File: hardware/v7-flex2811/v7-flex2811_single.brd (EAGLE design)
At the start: 7.8 x 7.8 mm, 8 parts

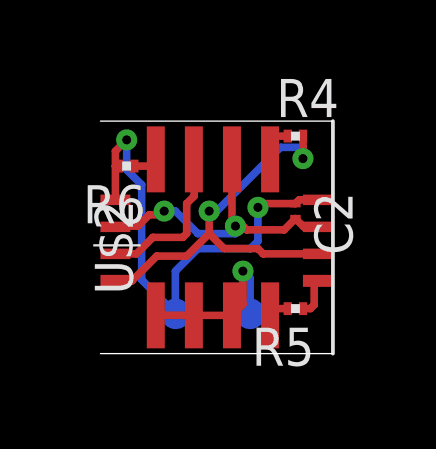
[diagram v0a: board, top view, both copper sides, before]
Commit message: Rework the single for more clearance to make fab easier
Was concerned about how tight the passives were for
assmebly, have just spread it out a bit

Also made the WS2818 pads slightly smaller so we have more clearance
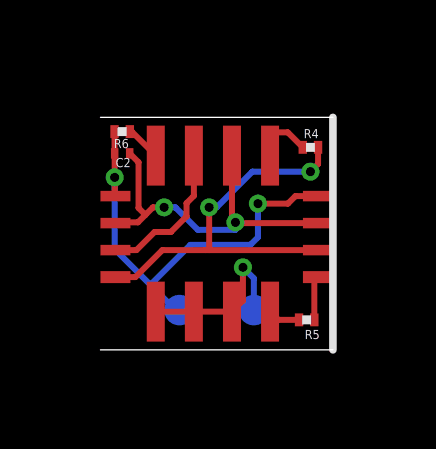
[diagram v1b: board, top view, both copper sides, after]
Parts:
- U$2: device adafruit:SO08 -> Sparky:SO08
- moved C2 6.09 mm to (0.72, 6.55), turned to 0 degrees
- moved R6 1.16 mm to (0.72, 7.28)
- moved R4 0.62 mm to (7.00, 6.75)
- moved R5 0.53 mm to (6.88, 1.00)
- moved U$1 0.18 mm to (3.88, 3.88)
- moved U$2 0.12 mm to (3.75, 3.88)
- moved U$3 0.12 mm to (0.50, 2.12)
- moved U$4 0.12 mm to (7.25, 2.12)
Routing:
- net GND: track 10.2 -> 12.1 mm
- net VCC: track 16.6 -> 15.0 mm
- net N$4: track 1.56 -> 2.27 mm

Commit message: More edit for manufacturability
Add a preliminary BOM
Add labels for the ICs for assembly
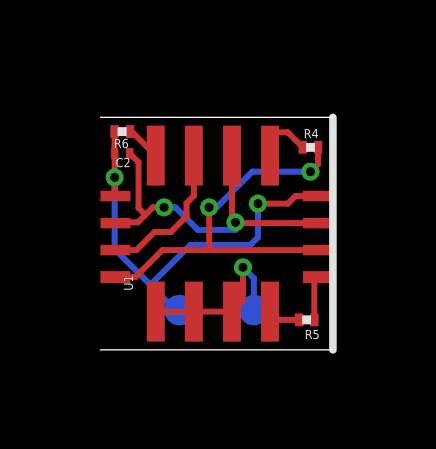
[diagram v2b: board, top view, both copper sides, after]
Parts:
- C2: value (none) -> 0.1uF
- R4, R5: value (none) -> 33Ω
- R6: value (none) -> 100Ω
- renumbered U$1 to P1, U$2 to U1
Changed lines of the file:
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@@
 <layer number="25" name="tNames" color="7" fill="1" visible="yes" active="yes"/>
 <layer number="26" name="bNames" color="7" fill="1" visible="yes" active="yes"/>
-<layer number="27" name="tValues" color="7" fill="1" visible="yes" active="yes"/>
-<layer number="28" name="bValues" color="7" fill="1" visible="yes" active="yes"/>
+<layer number="27" name="tValues" color="7" fill="1" visible="no" active="yes"/>
+<layer number="28" name="bValues" color="7" fill="1" visible="no" active="yes"/>
 <layer number="29" name="tStop" color="7" fill="3" visible="no" active="yes"/>
 <layer number="30" name="bStop" color="7" fill="6" visible="no" active="yes"/>
@@
 </autorouter>
 <elements>
-<element name="C2" library="rcl" package="C0201" value="" x="0.725" y="6.55" smashed="yes">
+<element name="C2" library="rcl" package="C0201" value="0.1uF" x="0.725" y="6.55" smashed="yes">
 <attribute name="NAME" x="0.505" y="6.09" size="0.3048" layer="25" font="vector" ratio="15"/>
 <attribute name="VALUE" x="0.09" y="4.645" size="1.27" layer="27"/>
 </element>
-<element name="U$1" library="tom-tappytap-v5-flex" package="TP_4MM_MED_PAD" value="TP_4MM_MED_PAD" x="3.875" y="3.875" smashed="yes" rot="MR0"/>
-<element name="U$2" library="Sparky" package="SO08" value="WS2818" x="3.75" y="3.875" smashed="yes"/>
-<element name="R4" library="rcl" package="R0201" value="" x="7" y="6.75" smashed="yes">
+<element name="P1" library="tom-tappytap-v5-flex" package="TP_4MM_MED_PAD" value="TP_4MM_MED_PAD" x="3.875" y="3.875" smashed="yes" rot="MR0"/>
+<element name="U1" library="Sparky" package="SO08" value="WS2818" x="3.75" y="3.875" smashed="yes">
+<attribute name="NAME" x="1.083" y="1.97" size="0.3048" layer="25" font="vector" ratio="15" rot="R90"/>
+<attribute name="VALUE" x="7.687" y="1.97" size="1.27" layer="27" rot="R90"/>
+</element>
+<element name="R4" library="rcl" package="R0201" value="33Ω" x="7" y="6.75" smashed="yes">
 <attribute name="NAME" x="6.775" y="7.055" size="0.3048" layer="25" font="vector" ratio="15"/>
 <attribute name="VALUE" x="6.365" y="4.845" size="1.27" layer="27"/>
 </element>
-<element name="R5" library="rcl" package="R0201" value="" x="6.875" y="1" smashed="yes" rot="R180">
+<element name="R5" library="rcl" package="R0201" value="33Ω" x="6.875" y="1" smashed="yes" rot="R180">
 <attribute name="NAME" x="7.31" y="0.665" size="0.3048" layer="25" font="vector" ratio="15" rot="R180"/>
 <attribute name="VALUE" x="7.51" y="2.905" size="1.27" layer="27" rot="R180"/>
 </element>
-<element name="R6" library="rcl" package="R0201" value="" x="0.725" y="7.275" smashed="yes" rot="R180">
+<element name="R6" library="rcl" package="R0201" value="100Ω" x="0.725" y="7.275" smashed="yes" rot="R180">
 <attribute name="NAME" x="0.445" y="6.725" size="0.3048" layer="25" font="vector" ratio="15"/>
 <attribute name="VALUE" x="1.36" y="9.18" size="1.27" layer="27" rot="R180"/>
@@
 <signal name="GND">
 <contactref element="C2" pad="2"/>
-<contactref element="U$2" pad="6"/>
+<contactref element="U1" pad="6"/>
 <contactref element="U$3" pad="P$3"/>
 <contactref element="U$4" pad="P$3"/>
@@
 </signal>
 <signal name="VCC">
-<contactref element="U$1" pad="P$2"/>
+<contactref element="P1" pad="P$2"/>
 <contactref element="C2" pad="1"/>
 <contactref element="R6" pad="2"/>
@@
 </signal>
 <signal name="NEG_PAD">
-<contactref element="U$1" pad="P$1"/>
-<contactref element="U$2" pad="3"/>
-<contactref element="U$2" pad="2"/>
-<contactref element="U$2" pad="1"/>
+<contactref element="P1" pad="P$1"/>
+<contactref element="U1" pad="3"/>
+<contactref element="U1" pad="2"/>
+<contactref element="U1" pad="1"/>
 <wire x1="1.845" y1="1.275" x2="3.115" y2="1.275" width="0.2" layer="1"/>
 <wire x1="3.115" y1="1.275" x2="4.385" y2="1.275" width="0.2" layer="1"/>
@@
 </signal>
 <signal name="N$4">
-<contactref element="U$2" pad="5"/>
+<contactref element="U1" pad="5"/>
 <contactref element="R4" pad="1"/>
 <wire x1="5.655" y1="6.775" x2="5.655" y2="6.475" width="0.2" layer="1"/>
@@
 </signal>
 <signal name="N$5">
-<contactref element="U$2" pad="4"/>
+<contactref element="U1" pad="4"/>
 <contactref element="R5" pad="2"/>
 <wire x1="5.655" y1="1.275" x2="5.93" y2="1" width="0.2" layer="1"/>
@@
 </signal>
 <signal name="N$6">
-<contactref element="U$2" pad="8"/>
+<contactref element="U1" pad="8"/>
 <contactref element="R6" pad="1"/>
 <wire x1="1.845" y1="6.775" x2="1.845" y2="6.475" width="0.2" layer="1"/>
@@
 </signal>
 <signal name="BIN">
-<contactref element="U$2" pad="7"/>
+<contactref element="U1" pad="7"/>
 <contactref element="U$3" pad="P$2"/>
 <wire x1="0.5" y1="3.325" x2="1.2" y2="3.325" width="0.2" layer="1"/>
